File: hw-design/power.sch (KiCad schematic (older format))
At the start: 10 parts, among them P3 CONN_01X03, SW1 SWITCH_INV, U1 usb-micro, U3 MCP73833, U4 MIC5501

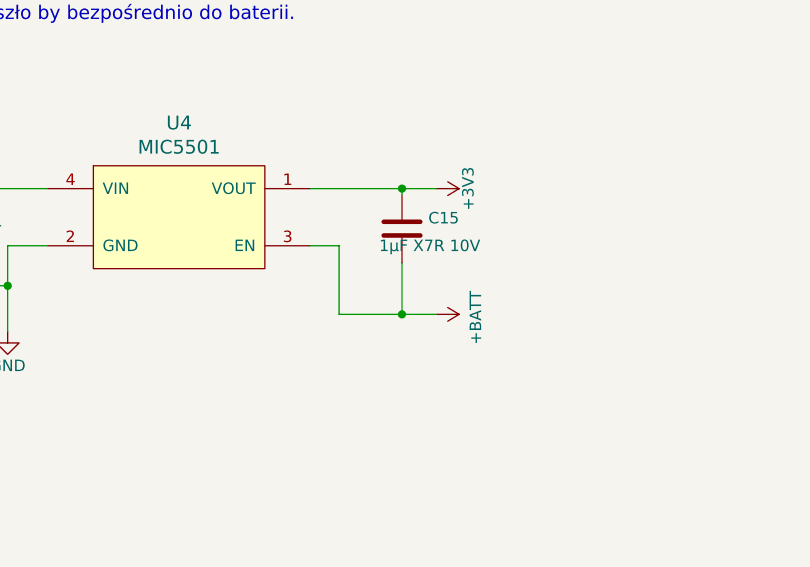
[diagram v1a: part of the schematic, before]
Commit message: Another idea of PCB split.
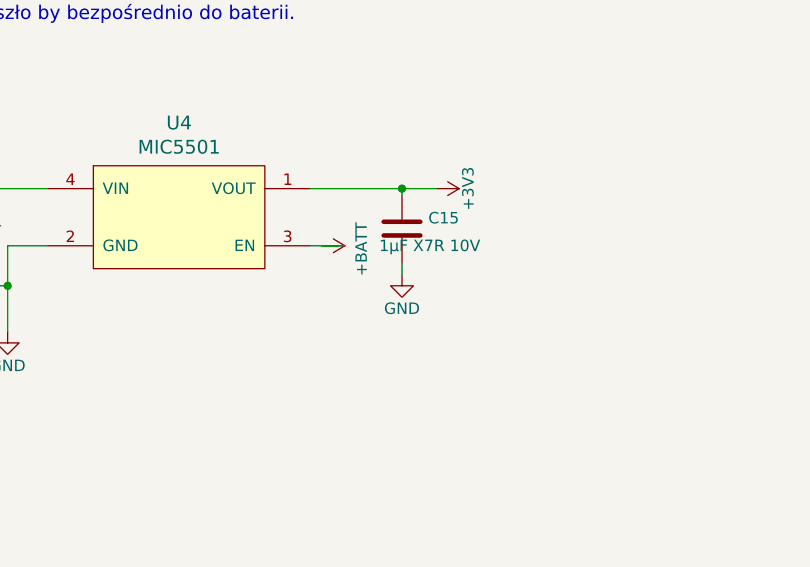
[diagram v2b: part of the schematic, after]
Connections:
- wire segments 38 -> 37
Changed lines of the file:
@@
 $Descr A4 11693 8268
 encoding utf-8
-Sheet 2 6
+Sheet 2 7
 Title ""
 Date ""
@@
 $EndComp
 $Comp
-L +3V3 #PWR9
+L +3V3 #PWR11
 U 1 1 5723EAD8
 P 10150 2925
-F 0 "#PWR9" H 10150 2775 50  0001 C CNN
+F 0 "#PWR11" H 10150 2775 50  0001 C CNN
 F 1 "+3V3" H 10150 3065 50  0000 C CNN
 F 2 "" H 10150 2925 60  0000 C CNN
@@
 Connection ~ 8000 2925
 $Comp
-L +BATT #PWR10
+L +BATT #PWR9
 U 1 1 580EB925
-P 10150 3475
-F 0 "#PWR10" H 10150 3325 50  0001 C CNN
-F 1 "+BATT" H 10165 3648 50  0000 C CNN
-F 2 "" H 10150 3475 50  0000 C CNN
-F 3 "" H 10150 3475 50  0000 C CNN
-	1    10150 3475
+P 9650 3175
+F 0 "#PWR9" H 9650 3025 50  0001 C CNN
+F 1 "+BATT" H 9665 3348 50  0000 C CNN
+F 2 "" H 9650 3175 50  0000 C CNN
+F 3 "" H 9650 3175 50  0000 C CNN
+	1    9650 3175
 	0    1    1    0
 $EndComp
@@
 	9600 3175 9725 3175
 Wire Wire Line
-	9725 3175 9725 3475
-Wire Wire Line
-	9725 3475 10150 3475
-Wire Wire Line
-	10000 3250 10000 3475
-Connection ~ 10000 3475
+	9650 3175 9750 3175
 Wire Wire Line
 	10000 2950 10000 2925
 Connection ~ 10000 2925
+$Comp
+L GND #PWR10
+U 1 1 580F6441
+P 10000 3300
+F 0 "#PWR10" H 10000 3050 50  0001 C CNN
+F 1 "GND" H 10000 3150 50  0000 C CNN
+F 2 "" H 10000 3300 60  0000 C CNN
+F 3 "" H 10000 3300 60  0000 C CNN
+	1    10000 3300
+	1    0    0    -1
+$EndComp
+Wire Wire Line
+	10000 3250 10000 3300
 $EndSCHEMATC
